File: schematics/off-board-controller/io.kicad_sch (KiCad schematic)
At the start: 44 parts, among them SW5 SW_SPDT_MSM, U8 MCP23S17_SP, U9 MCP23S17_SP

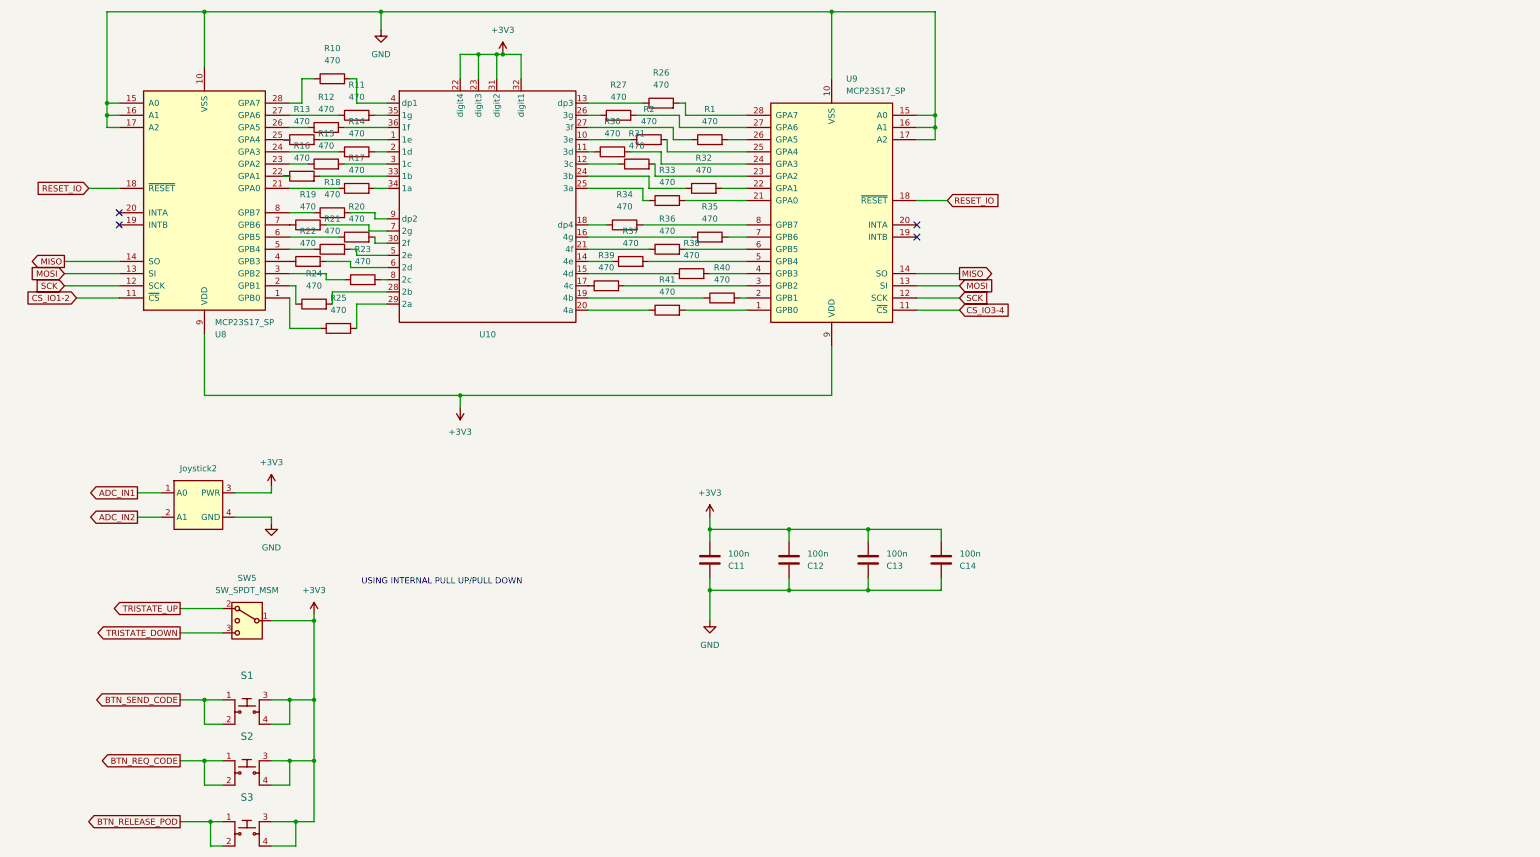
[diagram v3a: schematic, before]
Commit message: added some leds to controller
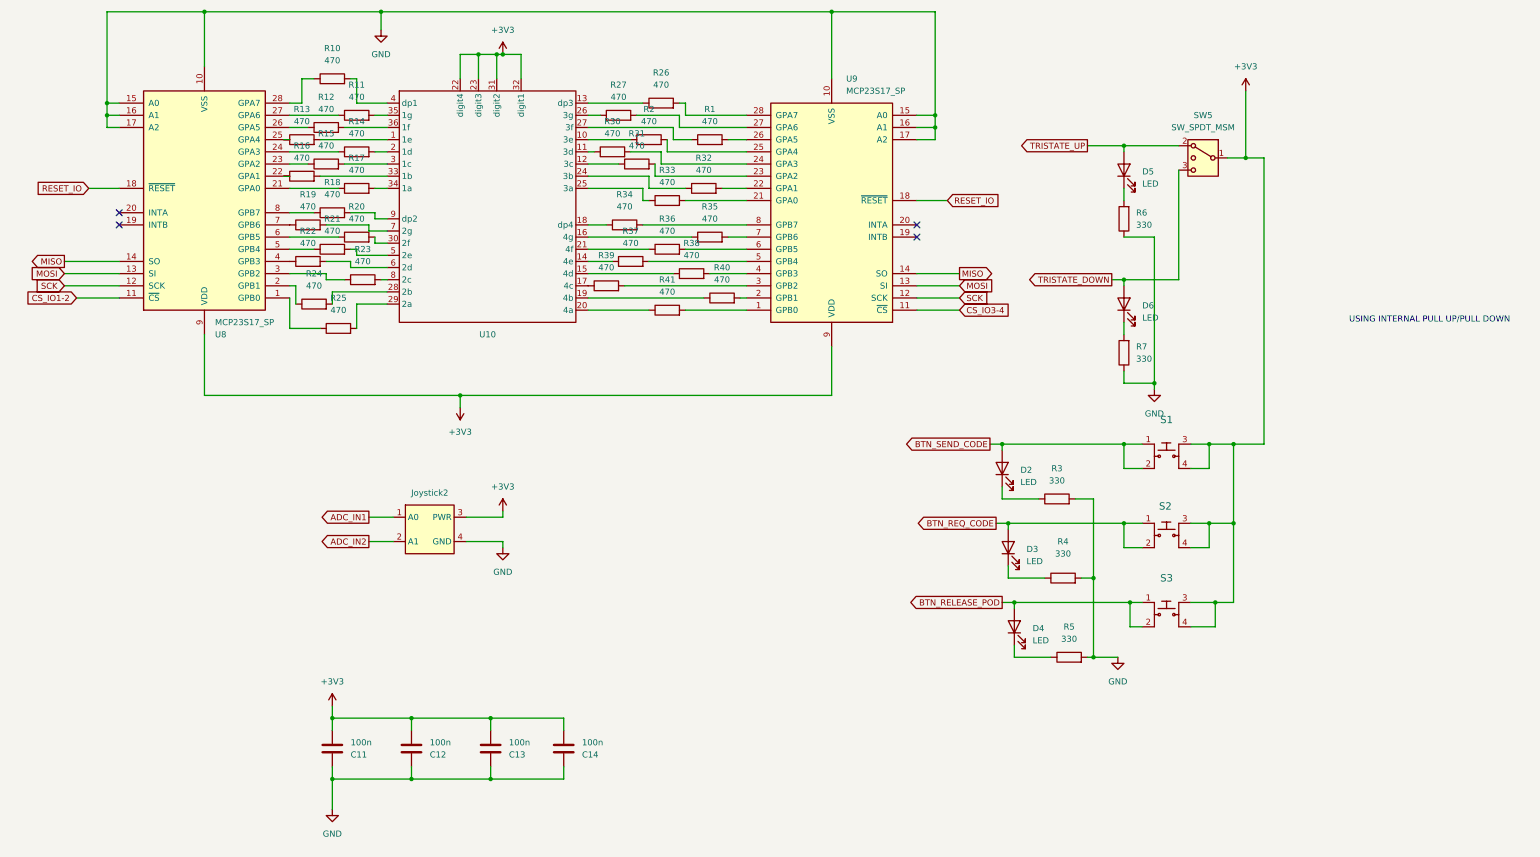
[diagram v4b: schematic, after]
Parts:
- added D2, D3, D4, D5, D6: LED, LED_SMD:LED_0805_2012Metric_Pad1.15x1.40mm_HandSolder, symbol Device:LED
- added R3, R4, R5, R6, R7: 330, Resistor_SMD:R_0805_2012Metric_Pad1.20x1.40mm_HandSolder, symbol Device:R
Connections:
- net BTN_RELEASE_POD: now also D4.2 (A)
- net BTN_REQ_CODE: now also D3.2 (A)
- net BTN_SEND_CODE: now also D2.2 (A)
- net GND: now also R3.2, R4.2, R5.2, R6.1, R7.1
- net TRISTATE_DOWN: now also D6.2 (A)
- net TRISTATE_UP: now also D5.2 (A)
- new net: D2.1 (K), R3.1
- new net: D3.1 (K), R4.1
- new net: D4.1 (K), R5.1
- new net: D5.1 (K), R6.2
- new net: D6.1 (K), R7.2
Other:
- moved on the sheet: C11, C12, C13, C14, Joystick2, S1, S2, S3, SW5

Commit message: produced first draft of layout design
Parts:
- removed C11, C13: 100n, Capacitor_SMD:C_0805_2012Metric_Pad1.18x1.45mm_HandSolder, symbol Device:C
- removed Joystick2: ~, Connector:NS-Tech_Grove_1x04_P2mm_Vertical, symbol New_Library:2DirJoystick
- added U1: ~, Connector:NS-Tech_Grove_1x04_P2mm_Vertical, symbol controller:joystick
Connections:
- net +3V3: now also U1.3 (PWR)
- net ADC_IN1: now also U1.1 (A0)
- net ADC_IN2: now also U1.2 (A1)
- net GND: now also U1.4 (GND)
